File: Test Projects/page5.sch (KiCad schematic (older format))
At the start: 29 parts, among them P13 CONN_01X08, P14 CONN_01X08, P15 CONN_01X08, P16 CONN_01X08, P17 CONN_01X08, P18 CONN_01X08, P19 CONN_01X08, P20 CONN_01X08, P21 CONN_01X07, U13 SF-4052, U14 SF-4052, U15 SF-4052, U16 SF-4052, U17 SF-4052, U18 SF-4052, U19 SF-4052, U20 SF-4052, U21 SF-4052, U22 SF-4052

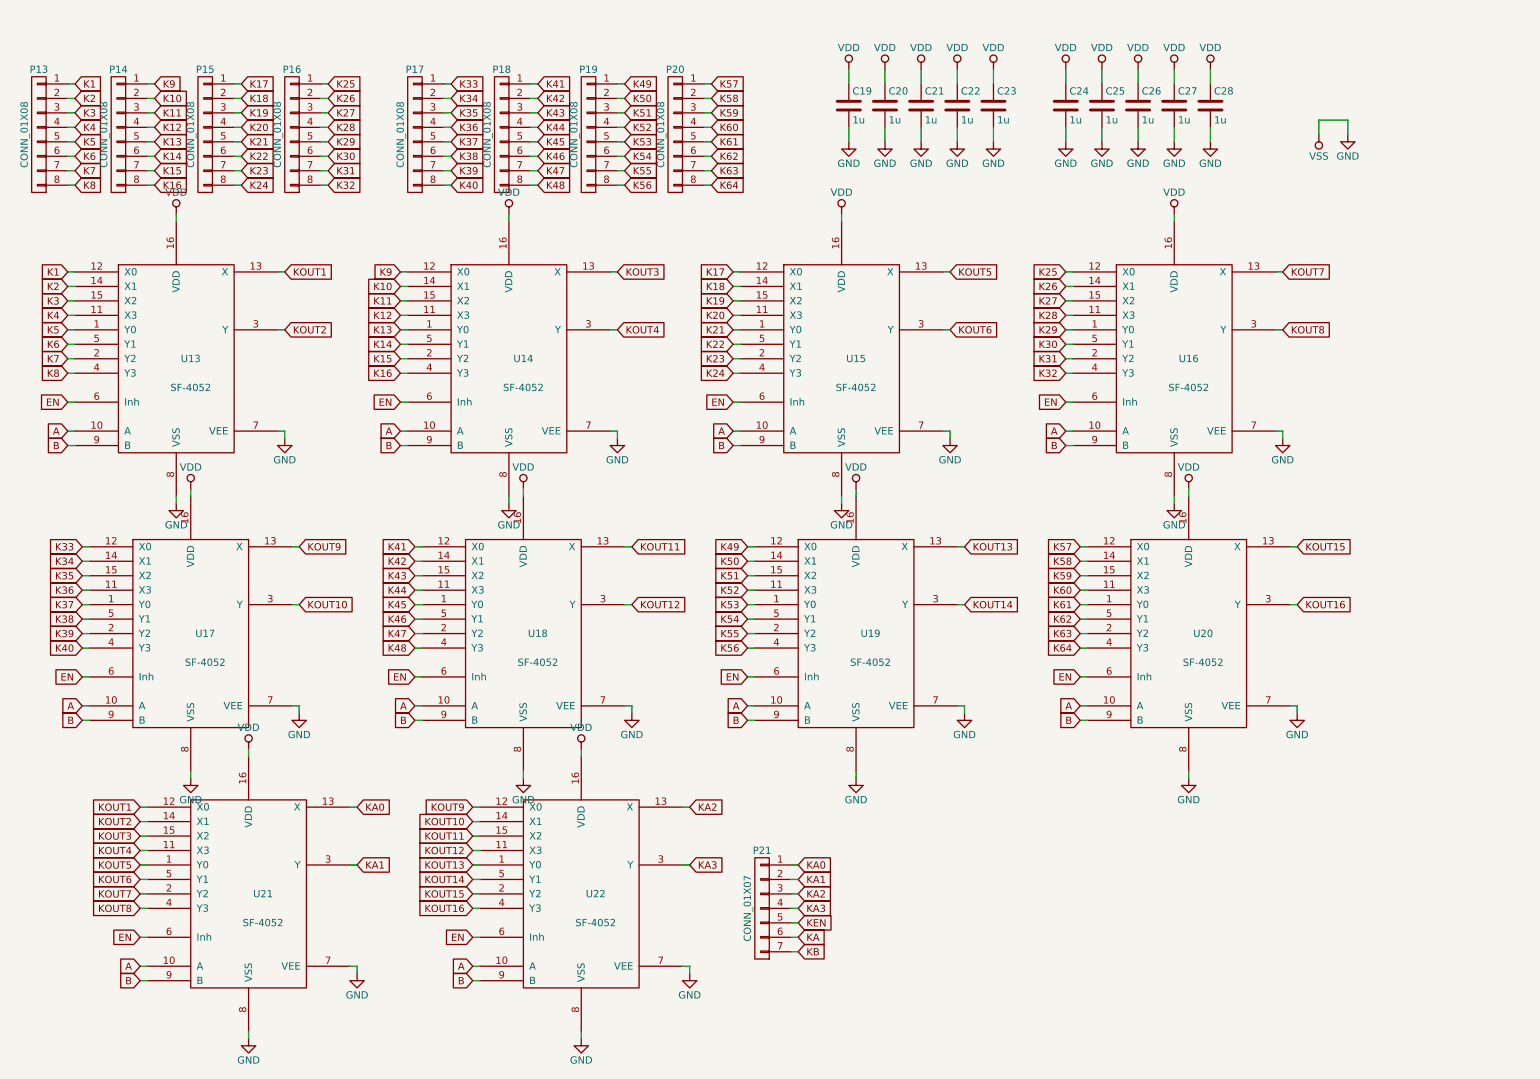
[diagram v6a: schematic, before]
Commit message: Added holes, moved layout
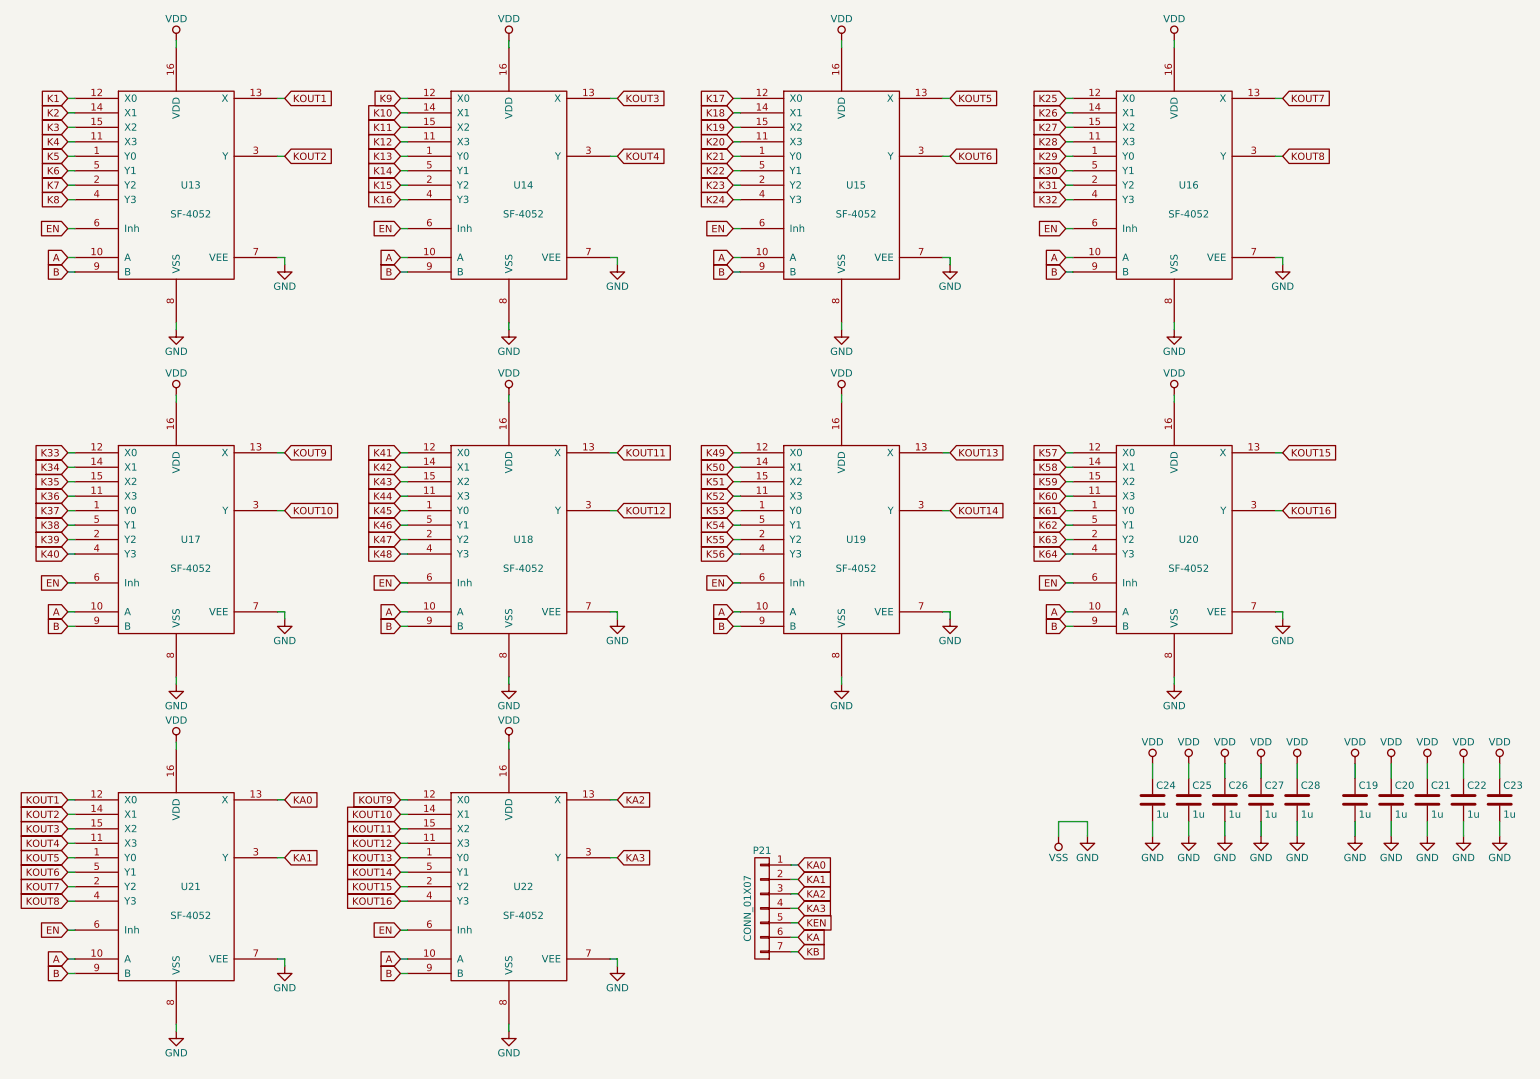
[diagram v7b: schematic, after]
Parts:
- removed P13, P14, P15, P16, P17, P18, P19, P20: CONN_01X08, Pin_Headers:Pin_Header_Straight_1x08, symbol CONN_01X08
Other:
- moved on the sheet: C19, C20, C21, C22, C23, C24, C25, C26, C27, C28, U13, U14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
